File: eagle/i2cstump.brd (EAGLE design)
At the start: 31.2 x 19 mm, 22 parts, among them IC1 ATTINY85, IC2 MCP1703CB, J1 I2C-5V, J2 I2C-3V3, J3 AVR_SPI_PROG_3X2TESTPOINTS, Q1 220mA/50V/3.5Ω, Q2 220mA/50V/3.5Ω, X1 USBPCB

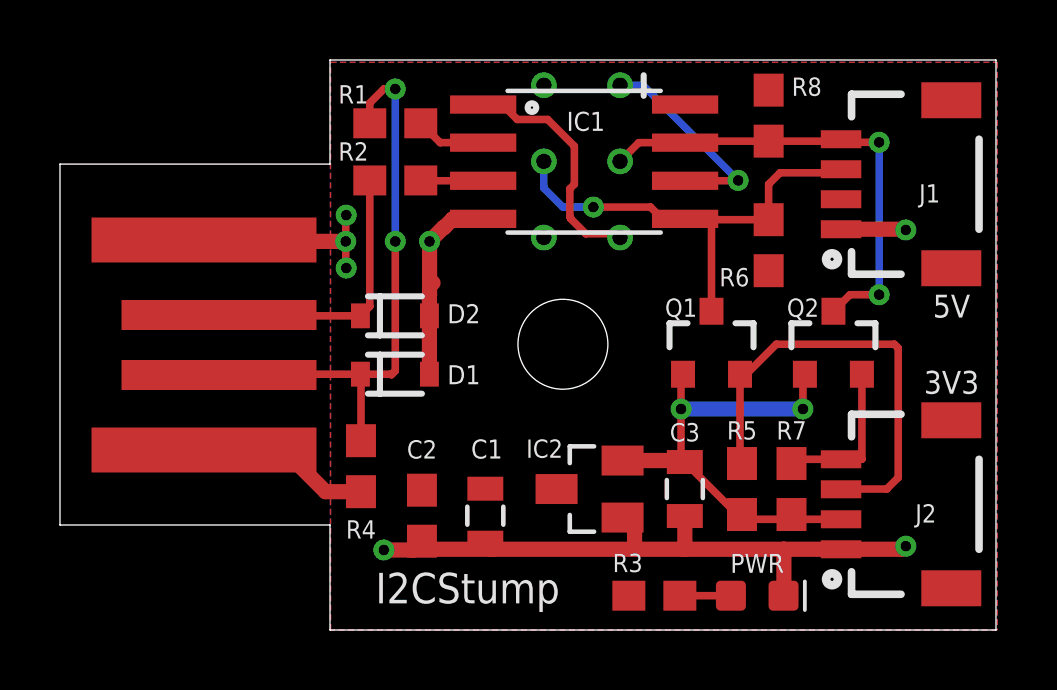
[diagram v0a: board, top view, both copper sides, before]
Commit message: Move R4 to align with C1/C2
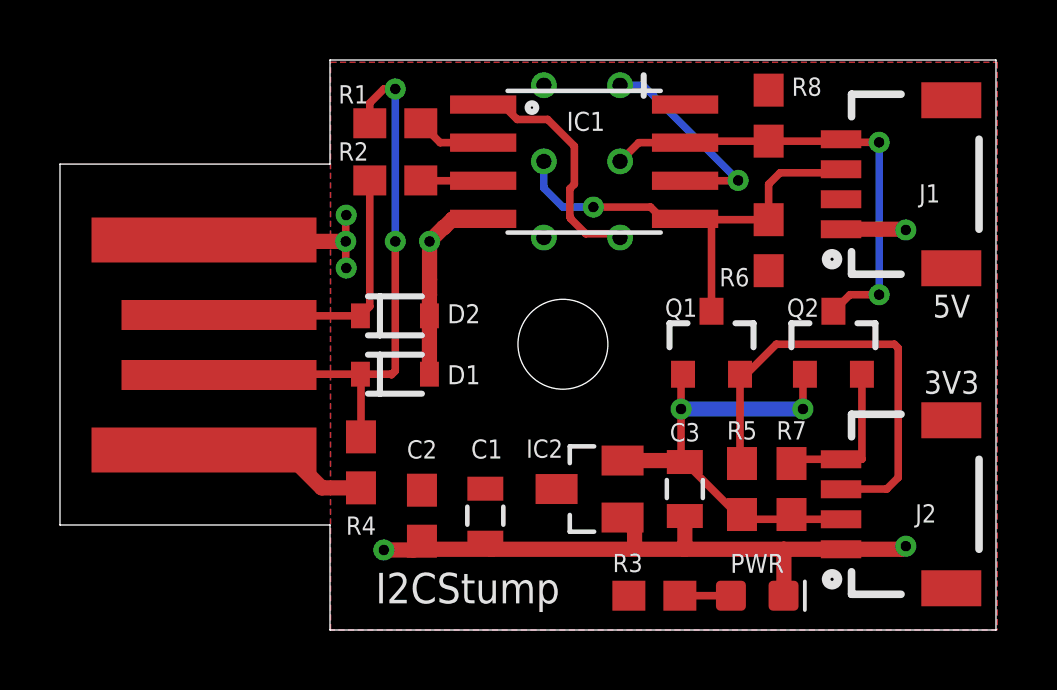
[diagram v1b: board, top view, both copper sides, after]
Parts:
- moved R4 0.13 mm to (10.0, 5.59)
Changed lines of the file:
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@@
 <setting verticaltext="up"/>
 </settings>
-<grid distance="0.005" unitdist="inch" unit="inch" style="lines" multiple="1" display="yes" altdistance="0.0025" altunitdist="inch" altunit="inch"/>
+<grid distance="0.005" unitdist="inch" unit="mil" style="lines" multiple="1" display="yes" altdistance="0.0025" altunitdist="inch" altunit="inch"/>
 <layers>
 <layer number="1" name="Top" color="4" fill="1" visible="yes" active="yes"/>
@@
 <attribute name="VALUE" x="24.384" y="17.145" size="0.6096" layer="27" font="vector" ratio="20" rot="R90" align="top-center"/>
 </element>
-<element name="R4" library="SparkFun-Resistors" library_urn="urn:adsk.eagle:library:532" package="0603" package3d_urn="urn:adsk.eagle:package:39650/1" value="2k2" x="10.033" y="5.461" smashed="yes" rot="R270">
-<attribute name="NAME" x="10.033" y="3.048" size="0.6096" layer="25" font="vector" ratio="20" align="bottom-center"/>
-<attribute name="PROD_ID" value=" " x="10.033" y="5.207" size="1.778" layer="27" rot="R270" display="off"/>
-<attribute name="VALUE" x="9.271" y="5.461" size="0.6096" layer="27" font="vector" ratio="20" rot="R270" align="top-center"/>
+<element name="R4" library="SparkFun-Resistors" library_urn="urn:adsk.eagle:library:532" package="0603" package3d_urn="urn:adsk.eagle:package:39650/1" value="2k2" x="10.033" y="5.588" smashed="yes" rot="R270">
+<attribute name="NAME" x="10.033" y="3.175" size="0.6096" layer="25" font="vector" ratio="20" align="bottom-center"/>
+<attribute name="PROD_ID" value=" " x="10.033" y="5.334" size="1.778" layer="27" rot="R270" display="off"/>
+<attribute name="VALUE" x="9.271" y="5.588" size="0.6096" layer="27" font="vector" ratio="20" rot="R270" align="top-center"/>
 </element>
 <element name="R1" library="SparkFun-Resistors" library_urn="urn:adsk.eagle:library:532" package="0603" package3d_urn="urn:adsk.eagle:package:39650/1" value="66R" x="11.176" y="16.891" smashed="yes" rot="R180">
@@
 <wire x1="9.906" y1="8.527" x2="5.327" y2="8.527" width="0.254" layer="1"/>
 <wire x1="5.327" y1="8.527" x2="5.3" y2="8.5" width="0.254" layer="1"/>
-<wire x1="10.033" y1="6.311" x2="10.033" y2="8.4" width="0.254" layer="1"/>
+<wire x1="10.033" y1="6.438" x2="10.033" y2="8.4" width="0.254" layer="1"/>
 <wire x1="10.033" y1="8.4" x2="9.906" y2="8.527" width="0.254" layer="1"/>
 <wire x1="10.326" y1="16.891" x2="10.326" y2="17.565" width="0.254" layer="1"/>
@@
 <wire x1="12.319" y1="11.684" x2="12.319" y2="11.176" width="0.508" layer="1"/>
 <wire x1="12.319" y1="11.176" x2="12.3145" y2="11.1715" width="0.508" layer="1"/>
-<wire x1="12.435" y1="11.568" x2="12.319" y2="11.684" width="0.508" layer="1"/>
 <wire x1="26.035" y1="2.691" x2="24.13" y2="2.691" width="0.508" layer="1"/>
 <wire x1="24.13" y1="2.691" x2="20.828" y2="2.691" width="0.508" layer="1"/>
@@
 <contactref element="X1" pad="5V"/>
 <contactref element="C2" pad="1"/>
-<wire x1="10.033" y1="4.611" x2="10.033" y2="4.699" width="0.508" layer="1"/>
 <contactref element="R3" pad="2"/>
 <polygon width="0.1524" layer="1">
@@
 <contactref element="J3" pad="2"/>
 <contactref element="IC2" pad="3"/>
-<wire x1="10.033" y1="4.611" x2="8.851" y2="4.611" width="0.508" layer="1"/>
-<wire x1="8.851" y1="4.611" x2="7.874" y2="5.588" width="0.508" layer="1"/>
+<wire x1="10.033" y1="4.738" x2="8.724" y2="4.738" width="0.508" layer="1"/>
+<wire x1="8.724" y1="4.738" x2="7.874" y2="5.588" width="0.508" layer="1"/>
 <wire x1="7.874" y1="5.588" x2="5.212" y2="5.588" width="0.508" layer="1"/>
 <wire x1="5.212" y1="5.588" x2="4.8" y2="6" width="0.508" layer="1"/>
